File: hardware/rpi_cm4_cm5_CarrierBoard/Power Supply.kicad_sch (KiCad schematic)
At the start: 99 parts, among them Q19 2N7002, Q2 2N7002, Q20 2N7002, Q3 2N7002, Q7 2N7002, U10 TPS54527DDAR, U11 TPS54527DDAR, U12 TPS7A7001DDAR, U13 INA180A2IDBVR, U14 INA180A2IDBVR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

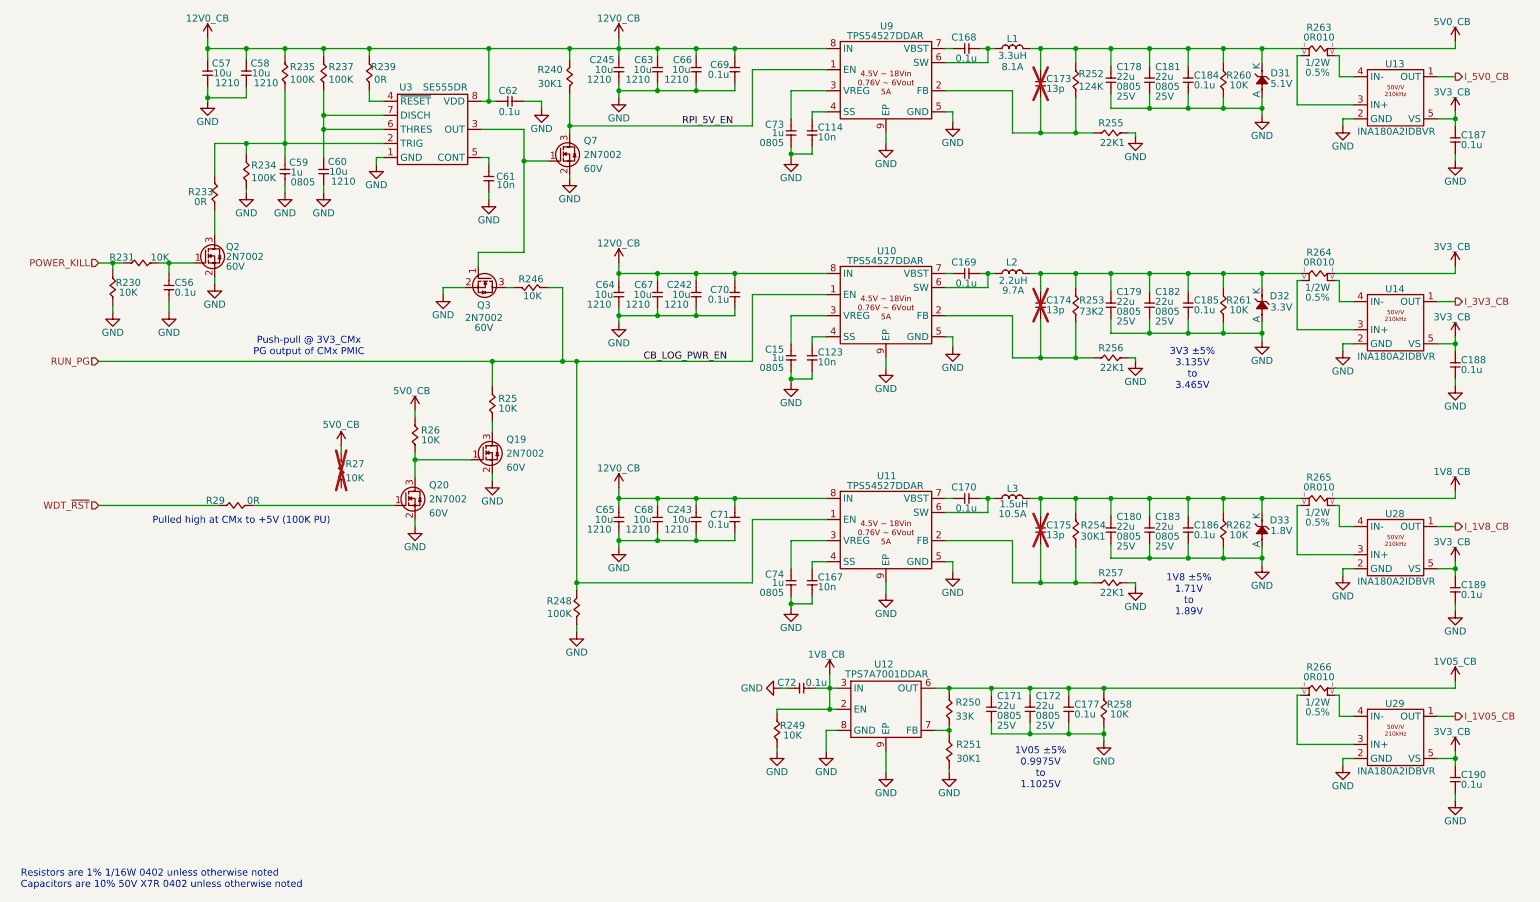
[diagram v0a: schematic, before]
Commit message: Finished implementation of watchdog circuit All possible reset scenarios documented
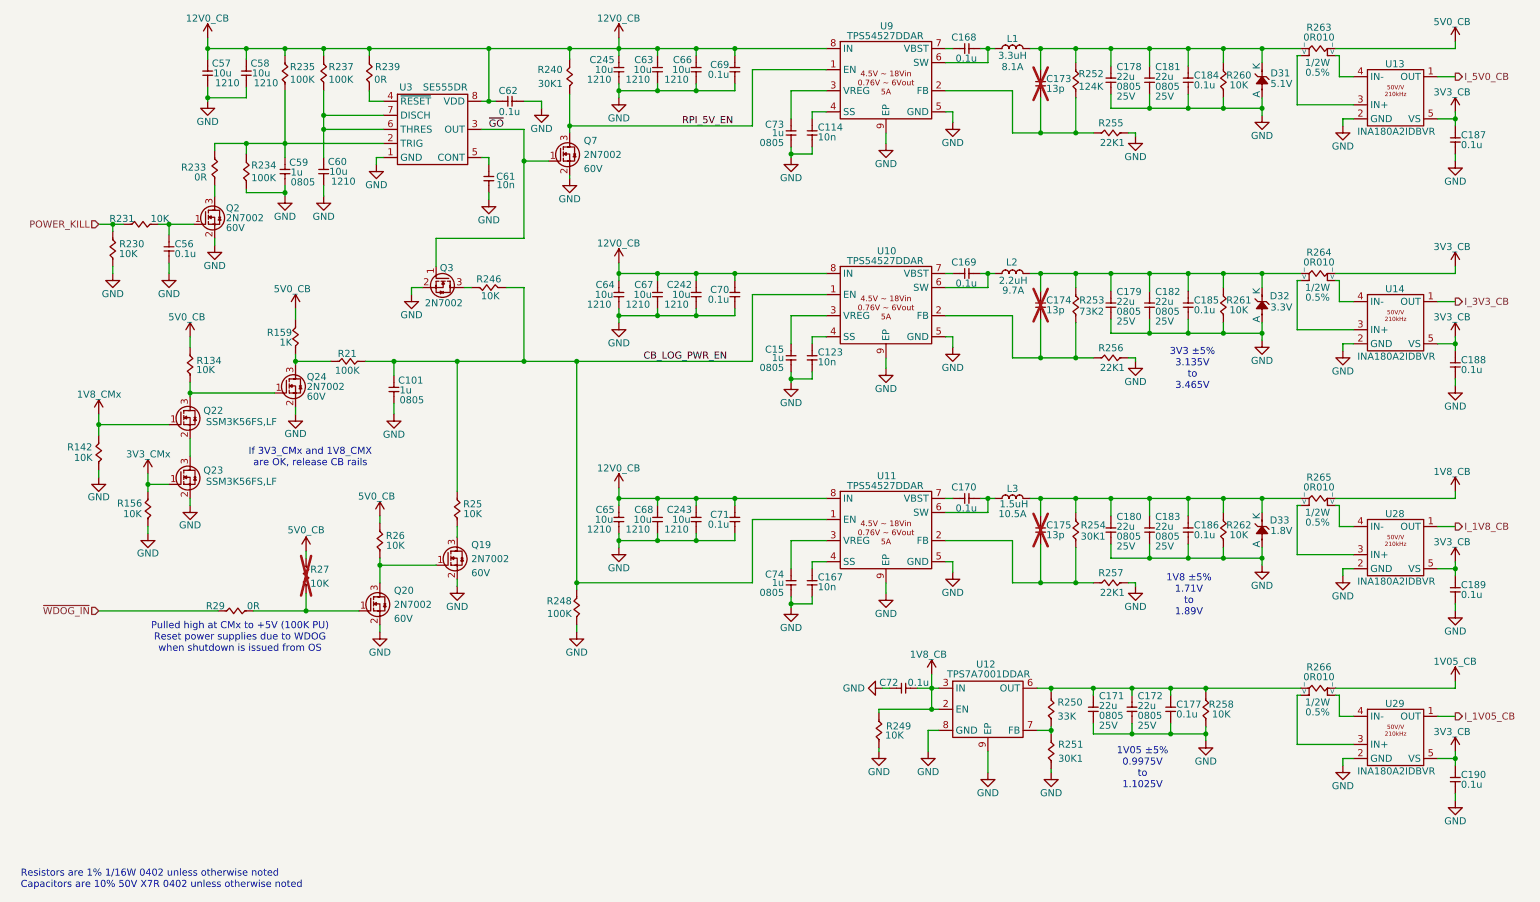
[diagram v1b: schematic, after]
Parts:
- added C101: 1u, footprint:CAP_NONPOL_0805, symbol KicadCompDb:Capacitors/CAP_CER_SMT_00002
- added Q22, Q23: SSM3K56FS,LF, footprint:SC-75, symbol KicadCompDb:Mosfet/MOSFET_00002
- added Q24: 2N7002, footprint:SOT-23-3, symbol KicadCompDb:Mosfet/MOSFET_00001
- added R134, R142, R156: 10K, footprint:RES_0402, symbol KicadCompDb:Resistors/RES_SMT_00013
- added R159: 1K, footprint:RES_0402, symbol KicadCompDb:Resistors/RES_SMT_00004
- added R21: 100K, footprint:RES_0402, symbol KicadCompDb:Resistors/RES_SMT_00018
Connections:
- net 5V0_CB: now also R134.2, R159.2
- net GND: now also C101.1, Q23.2 (S), Q24.2 (S), R142.1, R156.1
- net at R27.1: now also Q20.1 (G), R29.1
- net ~{GO}: now reaches Q3.1 (G), Q7.1 (G), U3.3 (OUT)
- net RUN_PG renamed CB_LOG_PWR_EN
- net CB_LOG_PWR_EN: now also C101.2, R21.1
- net WDT_~{RST} renamed ~{WDOG_IN}
- new net: Q24.3 (D), R159.1, R21.2
- new net: Q22.3 (D), Q24.1 (G), R134.1
- new net: Q22.2 (S), Q23.3 (D)
- new net 1V8_CMx: Q22.1 (G), R142.2
- new net 3V3_CMx: Q23.1 (G), R156.2
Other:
- note added: "If 3V3_CMx and 1V8_CMX are OK, release CB rails"
- note added: "Pulled high at CMx to +5V (100K PU) Reset power supplies due to WDOG when shutdown is issued from OS"
- note removed: "Pulled high at CMx to +5V (100K PU)"
- note removed: "Push-pull @ 3V3_CMx PG output of CMx PMIC"
- moved on the sheet: C171, C172, C177, C56, C72, Q19, Q2, Q20, Q3, R230, R231, R233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

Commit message: Update PCB design rules for outer layers differential pairs Update preliminary component placement Update schematics based on PCB placement & remove duplicata / unnecessary components Update design notes and power table
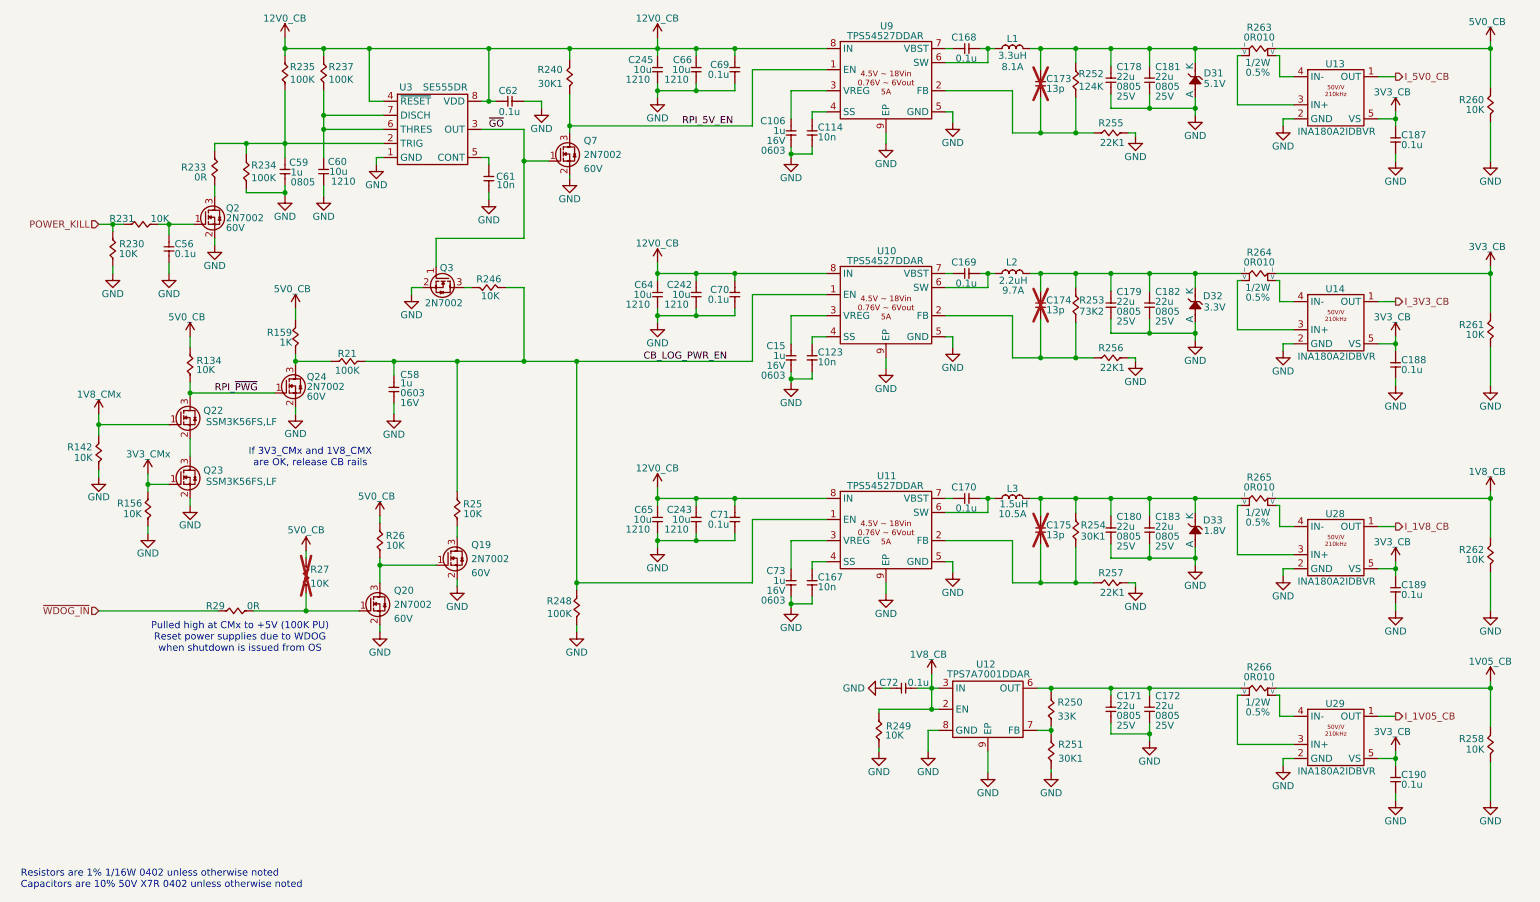
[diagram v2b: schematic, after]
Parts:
- removed C101, C15, C73, C74: 1u, footprint:CAP_NONPOL_0805, symbol KicadCompDb:Capacitors/CAP_CER_SMT_00002
- removed C177, C184, C185, C186: 0.1u, footprint:CAP_NONPOL_0402, symbol KicadCompDb:Capacitors/CAP_CER_SMT_00001
- removed C57, C58, C63, C67, C68: 10u, footprint:CAP_NONPOL_1210, symbol KicadCompDb:Capacitors/CAP_CER_SMT_00014
- removed R239: 0R, footprint:RES_0402, symbol KicadCompDb:Resistors/RES_SMT_00001
- added C106, C15, C58, C73: 1u, footprint:CAP_NONPOL_0603, symbol KicadCompDb:Capacitors/CAP_CER_SMT_00015
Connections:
- net 12V0_CB: now also U3.4 (~{RESET})
- net 1V05_CB: now also R258.2
- net 1V8_CB: now also R262.2
- net 3V3_CB: now also R261.2
- net 5V0_CB: now also R260.2
- net CB_LOG_PWR_EN: now also C58.2
- net GND: now also C106.1, C15.1, C58.1, C73.1
- net at U10.3 (VREG): now also C15.2
- net at C175.2, C180.2, C183.2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: no longer R262.2
- net at C171.2, C172.2, R250.2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: no longer R258.2
- net at C173.2, C178.2, C181.2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: no longer R260.2
- net at C174.2, C179.2, C182.2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: no longer R261.2
- net RPI_~{PWG}: now reaches Q22.3 (D), Q24.1 (G), R134.1
- net at U11.3 (VREG): now also C73.2
- net at U9.3 (VREG): now also C106.2
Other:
- note removed: "1V05 ±5% 0.9975V to 1.1025V"
- note removed: "1V8 ±5% 1.71V to 1.89V"
- note removed: "3V3 ±5% 3.135V to 3.465V"
- moved on the sheet: C171, C172, C187, C188, C189, C190, C245, C64, C65, D31, D32, D33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

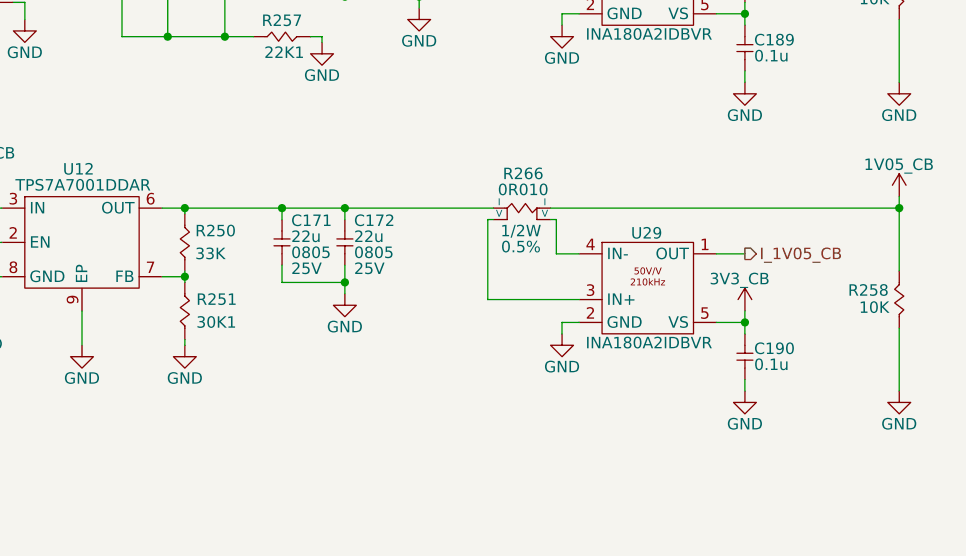
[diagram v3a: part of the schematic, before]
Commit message: Continue working on the layout. Completed most of power planes planning and pouring Completed all DiffPairs routing and length matching (preliminary)
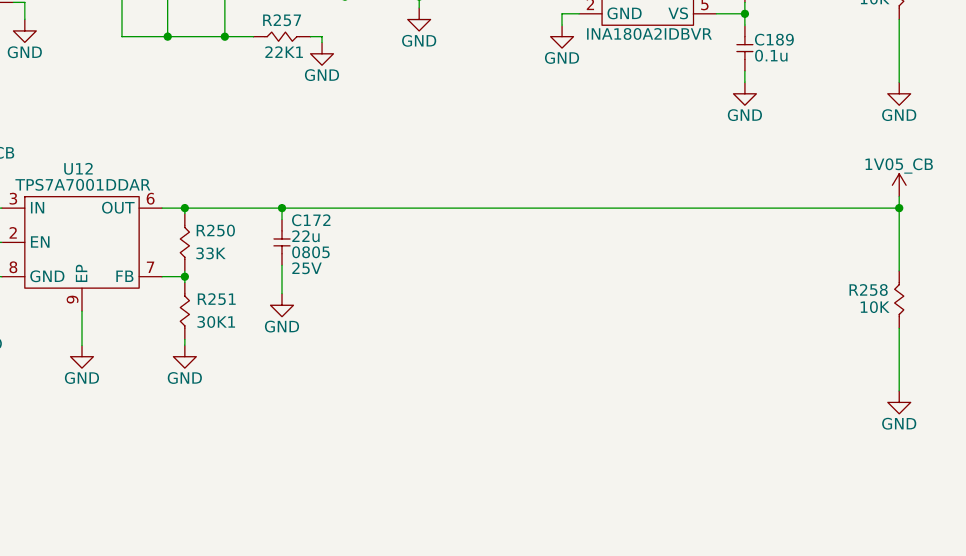
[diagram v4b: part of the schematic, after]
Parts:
- removed C171: 22u, footprint:CAP_NONPOL_0805, symbol KicadCompDb:Capacitors/CAP_CER_SMT_00011
- removed C190: 0.1u, footprint:CAP_NONPOL_0402, symbol KicadCompDb:Capacitors/CAP_CER_SMT_00001
- removed R266: 0R010, footprint:RES_SENSE_1206, symbol KicadCompDb:Resistors/RES_SMT_00033
- removed U29: INA180A2IDBVR, footprint:SOT-23-5, symbol KicadCompDb:Amplifier/AMP_00001
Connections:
- net 1V05_CB: now also C172.2, R250.2, U12.6 (OUT)
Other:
- moved on the sheet: C172
